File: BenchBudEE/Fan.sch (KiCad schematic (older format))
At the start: 7 parts

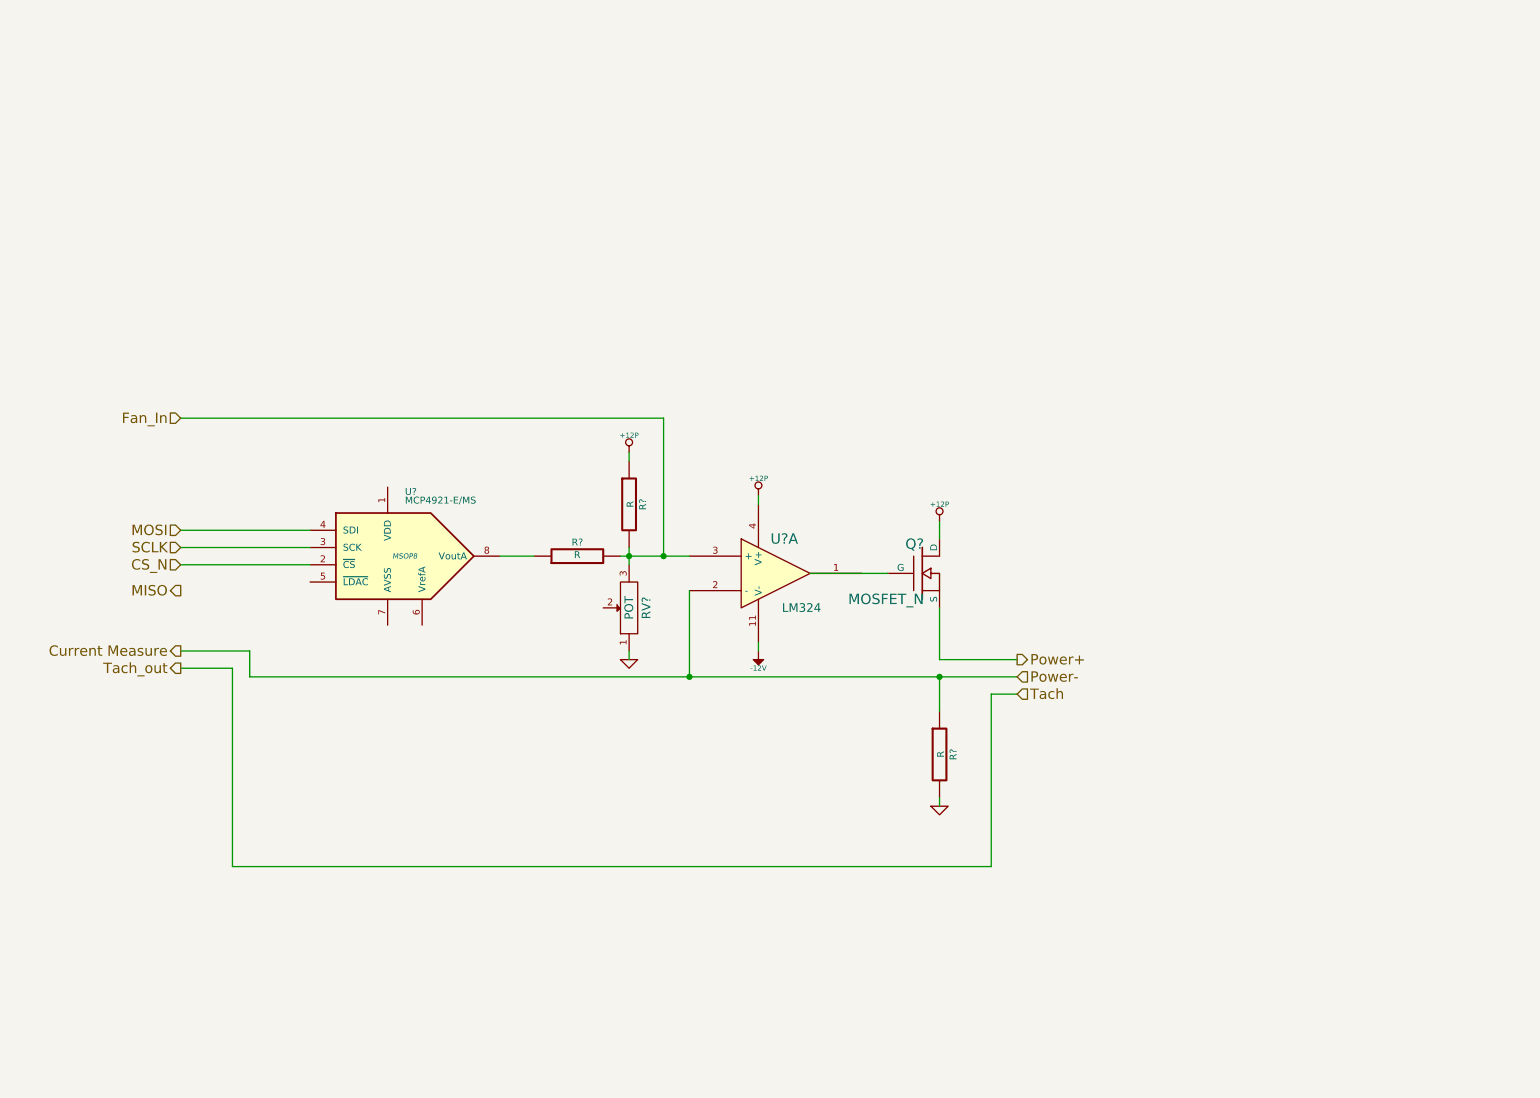
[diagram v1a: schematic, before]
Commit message: Completing schematics from week 3 videos.
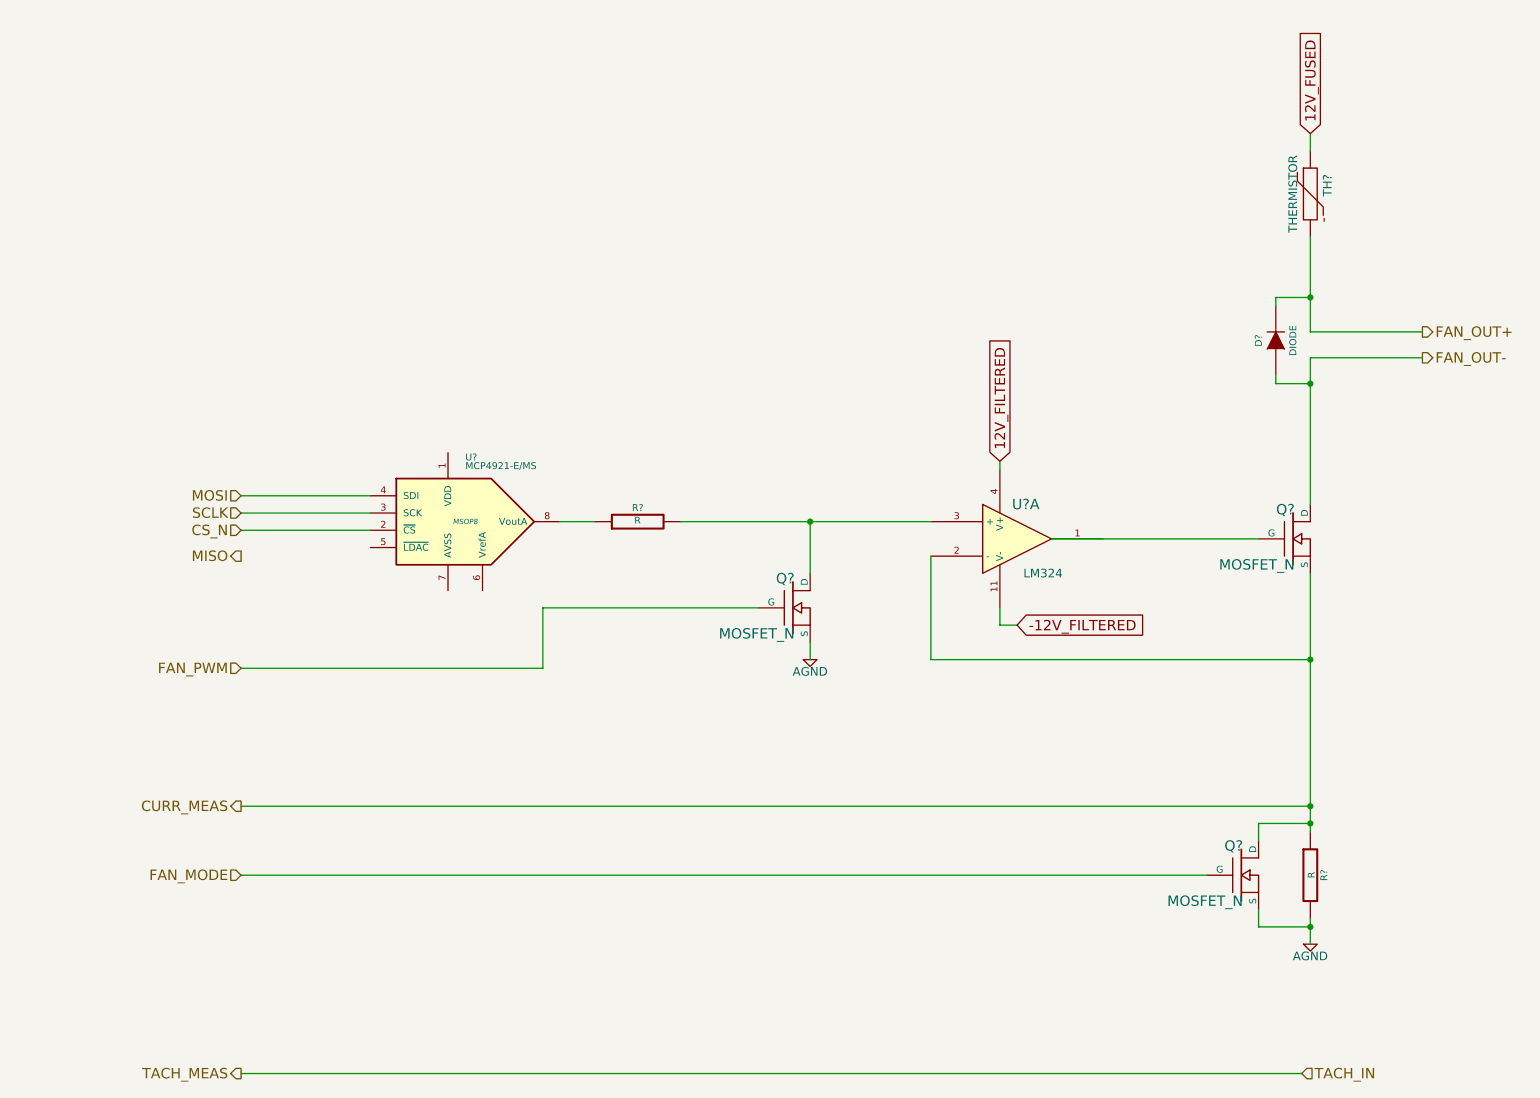
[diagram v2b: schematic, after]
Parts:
- removed R? (x2): R, ~, symbol R
- removed RV?: POT, ~, symbol POT
- added D?: DIODE, ~, symbol DIODE
- added Q? (x2): MOSFET_N, ~, symbol MOSFET_N
- added R?: R, ~, symbol R
- added TH?: THERMISTOR, ~, symbol THERMISTOR
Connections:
- net labels added: -12V_FILTERED, 12V_FILTERED, 12V_FUSED, AGND, CURR_MEAS, FAN_MODE, FAN_OUT+, FAN_OUT-, FAN_PWM, TACH_IN, TACH_MEAS
- net labels removed: +12P, -12V, Current Measure, Fan_In, GND, Power+, Power-, Tach, Tach_out
- wire segments 27 -> 34
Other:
- moved on the sheet: Q?, R?, U?, U?A

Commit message: checking in all my local changes before syncing to chris's repo.
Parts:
- gave numbers to parts that had none: 9
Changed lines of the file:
@@
 Sheet 6 9
 Title ""
-Date "24 feb 2014"
+Date "2 mar 2014"
 Rev ""
 Comp ""
@@
 TACH_MEAS
 $Comp
-L LM324 U?
+L LM324 U7
 U 1 1 52F82C69
 P 7250 3550
-F 0 "U?" H 7300 3750 60  0000 C CNN
+F 0 "U7" H 7300 3750 60  0000 C CNN
 F 1 "LM324" H 7400 3350 50  0000 C CNN
 F 2 "" H 7250 3550 60  0000 C CNN
@@
 $EndComp
 $Comp
-L MOSFET_N Q?
+L MOSFET_N Q4
 U 1 1 52F82C78
 P 8850 3550
-F 0 "Q?" H 8860 3720 60  0000 R CNN
+F 0 "Q4" H 8860 3720 60  0000 R CNN
 F 1 "MOSFET_N" H 8860 3400 60  0000 R CNN
 F 2 "~" H 8850 3550 60  0000 C CNN
@@
 	7150 3950 7150 4050
 $Comp
-L MCP4921-E/MS U?
+L MCP4921-E/MS U6
 U 1 1 52F82D97
 P 4050 3450
-F 0 "U?" H 4050 3800 40  0000 L BNN
+F 0 "U6" H 4050 3800 40  0000 L BNN
 F 1 "MCP4921-E/MS" H 4050 3750 40  0000 L BNN
 F 2 "MSOP8" H 4050 3450 30  0000 C CIN
@@
 	5300 3450 6750 3450
 $Comp
-L R R?
+L R R17
 U 1 1 52F82EA4
 P 5050 3450
-F 0 "R?" V 5130 3450 40  0000 C CNN
+F 0 "R17" V 5130 3450 40  0000 C CNN
 F 1 "R" V 5057 3451 40  0000 C CNN
 F 2 "~" V 4980 3450 30  0000 C CNN
@@
 12V_FUSED
 $Comp
-L THERMISTOR TH?
+L THERMISTOR TH6
 U 1 1 53094D63
 P 8950 1550
-F 0 "TH?" V 9050 1600 50  0000 C CNN
+F 0 "TH6" V 9050 1600 50  0000 C CNN
 F 1 "THERMISTOR" V 8850 1550 50  0000 C CNN
 F 2 "~" H 8950 1550 60  0000 C CNN
@@
 	8950 2500 8950 3350
 $Comp
-L DIODE D?
+L DIODE D5
 U 1 1 53094E00
 P 8750 2400
-F 0 "D?" H 8750 2500 40  0000 C CNN
+F 0 "D5" H 8750 2500 40  0000 C CNN
 F 1 "DIODE" H 8750 2300 40  0000 C CNN
 F 2 "~" H 8750 2400 60  0000 C CNN
@@
 	7150 4050 7250 4050
 $Comp
-L MOSFET_N Q?
+L MOSFET_N Q2
 U 1 1 53094EDB
 P 5950 3950
-F 0 "Q?" H 5960 4120 60  0000 R CNN
+F 0 "Q2" H 5960 4120 60  0000 R CNN
 F 1 "MOSFET_N" H 5960 3800 60  0000 R CNN
 F 2 "~" H 5950 3950 60  0000 C CNN
@@
 $EndComp
 $Comp
-L AGND #PWR?
+L AGND #PWR24
 U 1 1 53094EE3
 P 6050 4250
-F 0 "#PWR?" H 6050 4250 40  0001 C CNN
+F 0 "#PWR24" H 6050 4250 40  0001 C CNN
 F 1 "AGND" H 6050 4180 50  0000 C CNN
 F 2 "" H 6050 4250 60  0000 C CNN
@@
 	4500 4300 2750 4300
 $Comp
-L R R?
+L R R18
 U 1 1 53094F45
 P 8950 5500
-F 0 "R?" V 9030 5500 40  0000 C CNN
+F 0 "R18" V 9030 5500 40  0000 C CNN
 F 1 "R" V 8957 5501 40  0000 C CNN
 F 2 "~" V 8880 5500 30  0000 C CNN
@@
 $EndComp
 $Comp
-L MOSFET_N Q?
+L MOSFET_N Q3
 U 1 1 53094F66
 P 8550 5500
-F 0 "Q?" H 8560 5670 60  0000 R CNN
+F 0 "Q3" H 8560 5670 60  0000 R CNN
 F 1 "MOSFET_N" H 8560 5350 60  0000 R CNN
 F 2 "~" H 8550 5500 60  0000 C CNN
@@
 $EndComp
 $Comp
-L AGND #PWR?
+L AGND #PWR25
 U 1 1 53094F6E
 P 8950 5900
-F 0 "#PWR?" H 8950 5900 40  0001 C CNN
+F 0 "#PWR25" H 8950 5900 40  0001 C CNN
 F 1 "AGND" H 8950 5830 50  0000 C CNN
 F 2 "" H 8950 5900 60  0000 C CNN
